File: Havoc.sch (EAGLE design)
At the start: 21 parts, among them T1 2N3904, T2 2N3904, T3 2N3904, U1 ATMEGA328P_PDIP, U2 FT231XS, Y1 16MHz

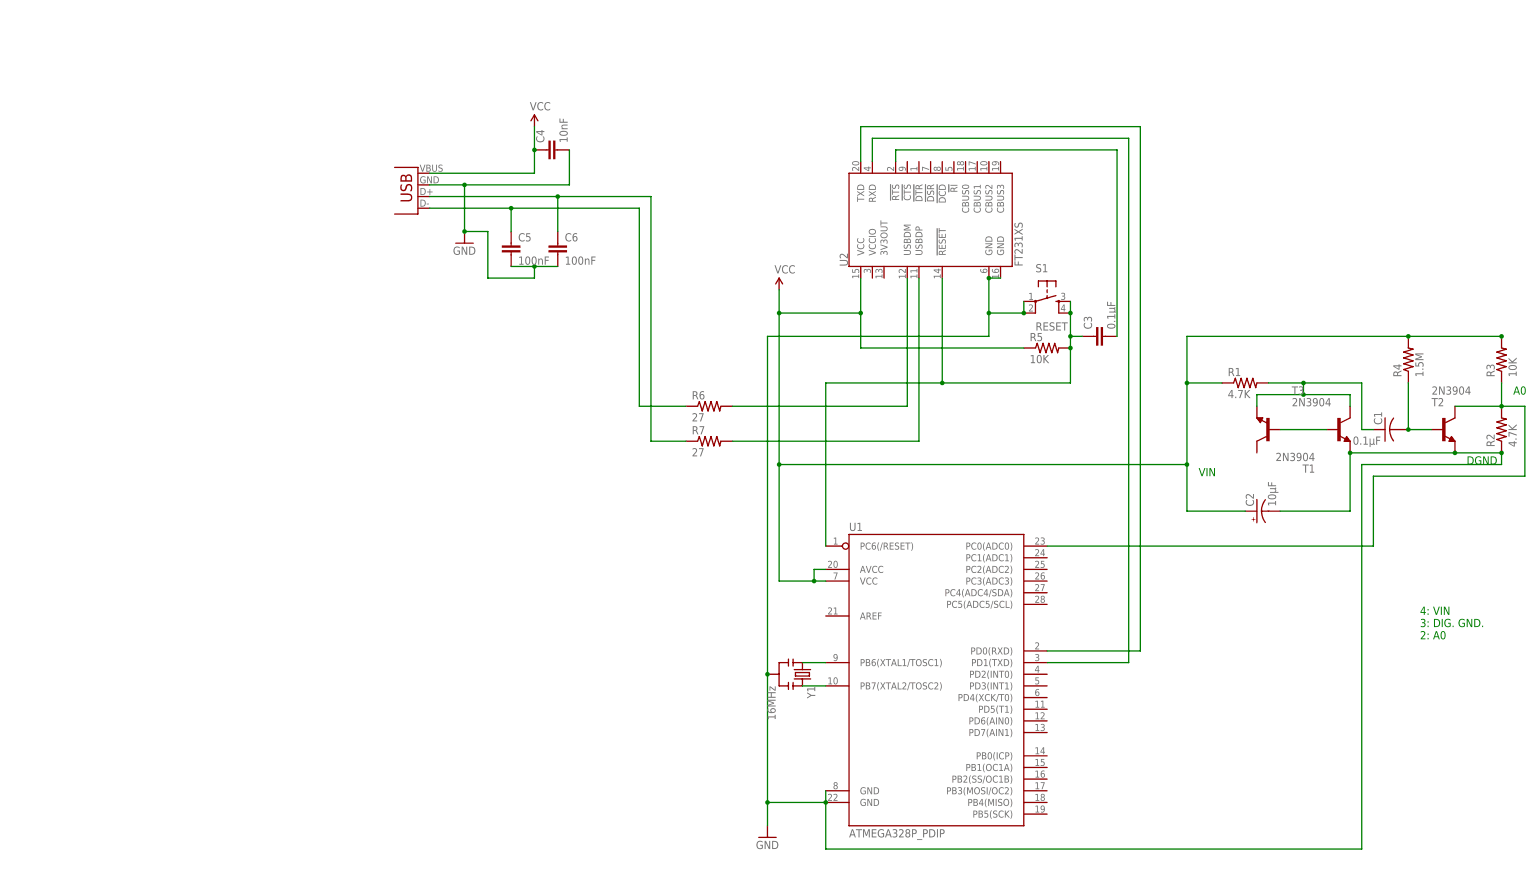
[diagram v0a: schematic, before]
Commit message: Switch to crystal and USB mini-B.
The crystal provides a more accurate clock, and USB mini-B turns
the project into a box. Using PTH components, it seems like a better
profile to use.
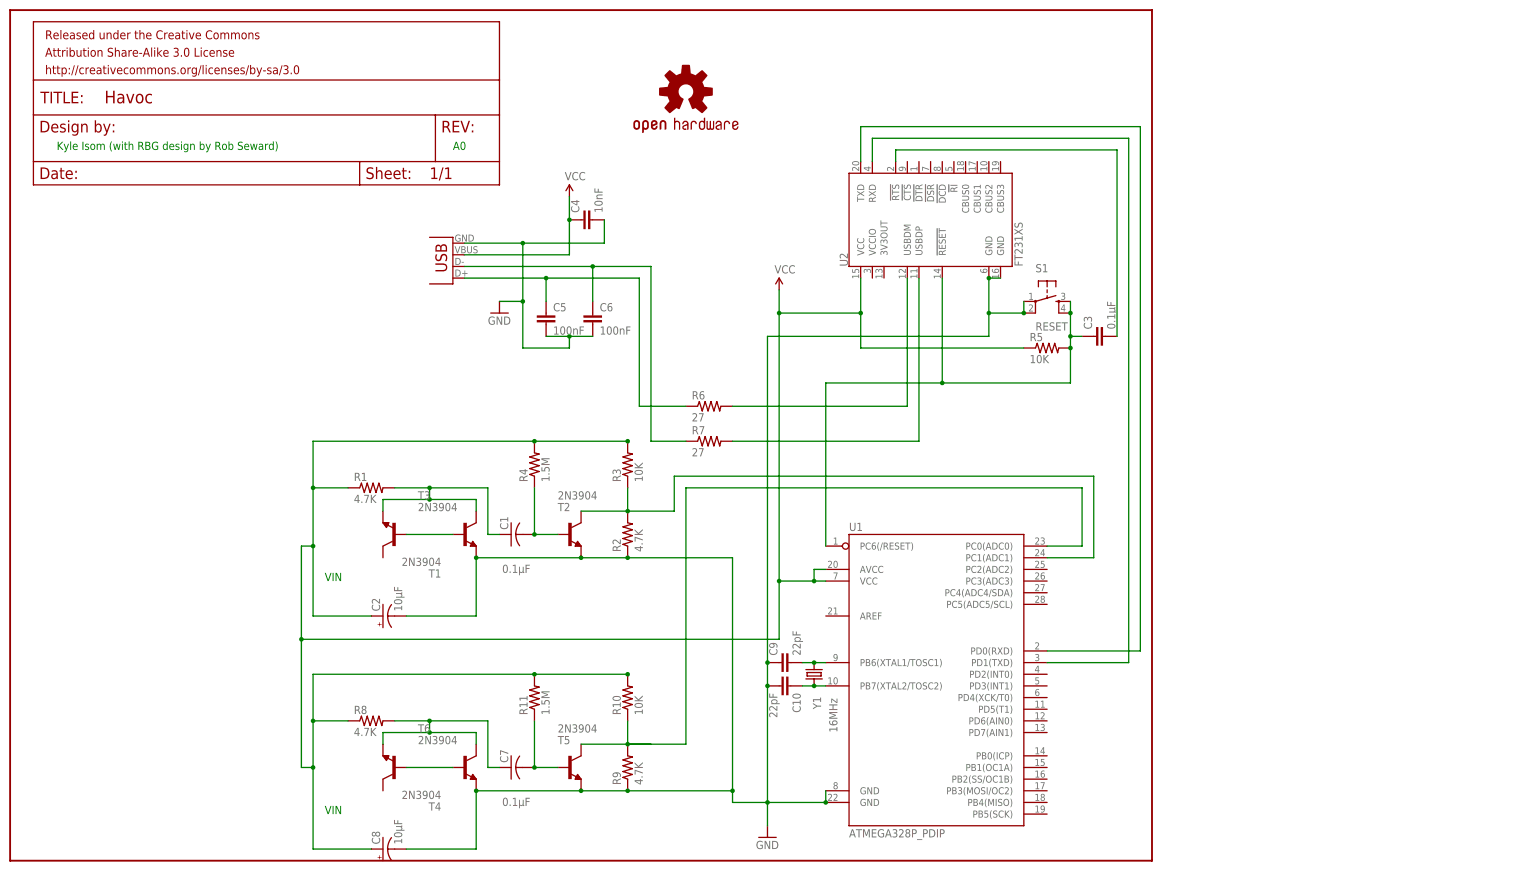
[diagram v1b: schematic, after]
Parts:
- added C10, C9: 22pF, SparkFun-Capacitors:CAPPTH
- added C7: 0.1µF, resistor:C-US050-030X075
- added C8: 10µF, resistor:CPOL-USE2-5
- added FRAME1: FRAME-LETTER, SparkFun-Aesthetics:FRAME-LETTER
- added LOGO1: OSHW-LOGOM, SparkFun-Aesthetics:OSHW-LOGOM
- added R10: 10K, resistor:R-US_0207/7
- added R11: 1.5M, resistor:R-US_0207/7
- added R8, R9: 4.7K, resistor:R-US_0207/7
- added T4, T5, T6: 2N3904, transistor:2N3904
- JP1: value USB-A-H -> USBSMD; device SparkFun-Connectors:USB-A-H -> SparkFun-Connectors:USBSMD
- Y1: device SparkFun-FreqCtrl:RESONATORPTH -> SparkFun-FreqCtrl:CRYSTALHC49US
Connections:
- new net N$17: T4.B, T6.B
- new net N$18: C7.1, R8.2, T4.E, T6.C
- new net N$19: R10.1, R9.2, T5.C, U1.PC0(ADC0)
- new net N$20: C7.2, R11.1, T5.B
- net GND: now also C10.2, C8.-, C9.1, JP1.GND, R9.1, T5.E, T6.E; no longer JP1.VBUS, Y1.2
- net N$1: now also C9.2, Y1.2; no longer Y1.1
- net N$2: now also C10.1, Y1.1; no longer Y1.3
- net N$7: now also U1.PC1(ADC1); no longer U1.PC0(ADC0)
- net VCC: now also C8.+, JP1.VBUS, R10.2, R11.2, R8.1; no longer JP1.GND
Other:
- note added: "Kyle Isom (with RBG design by Rob Seward)"
- note removed: "4: VIN 3: DIG. GND. 2: A0"
- note removed: "DGND"
- moved on the sheet: C1, C2, C4, C5, C6, R1, R2, R3, R4, T1, T2, T3
